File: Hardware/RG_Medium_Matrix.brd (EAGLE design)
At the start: 45.7 x 48.3 mm, 24 parts, among them IC1 74LS595D, IC2 74LS595D, U2 AVR_SPI_PRG_6PTH, U3 16MHz

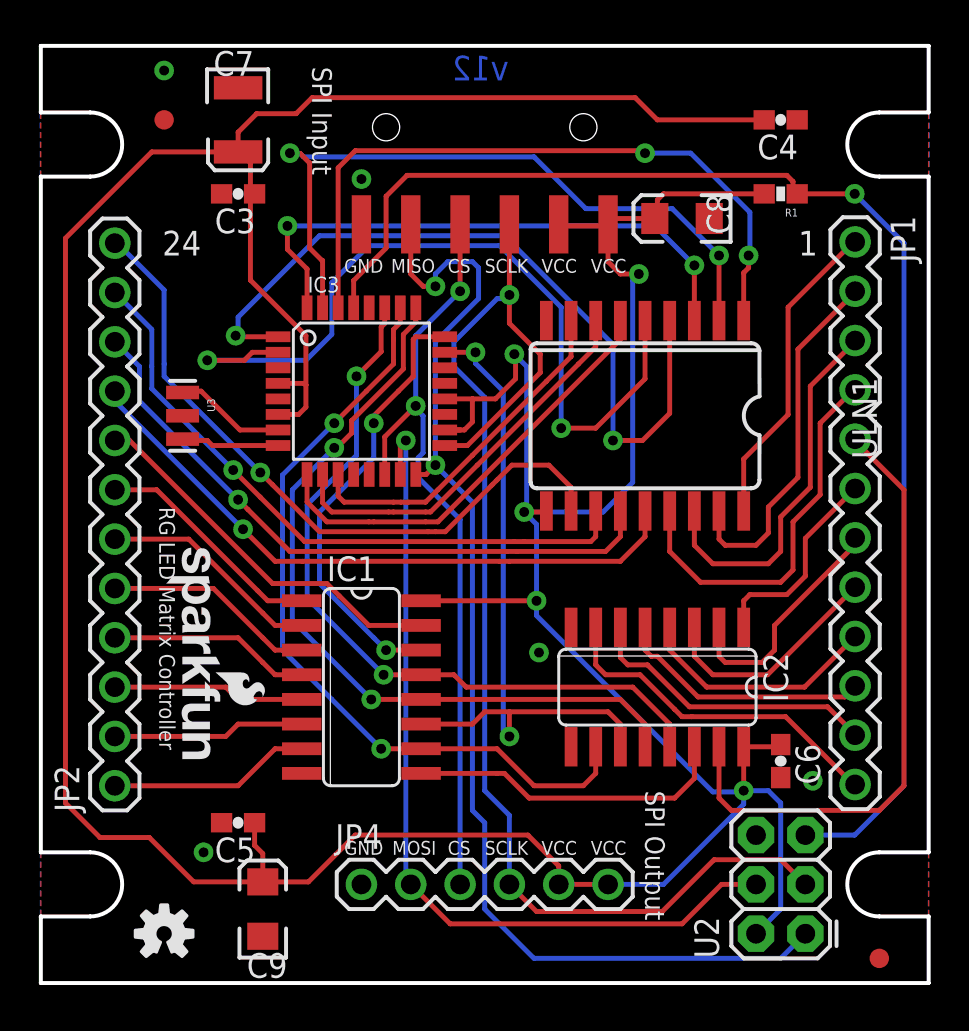
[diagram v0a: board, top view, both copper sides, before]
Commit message: Updating to locking footprints for SPI connectors
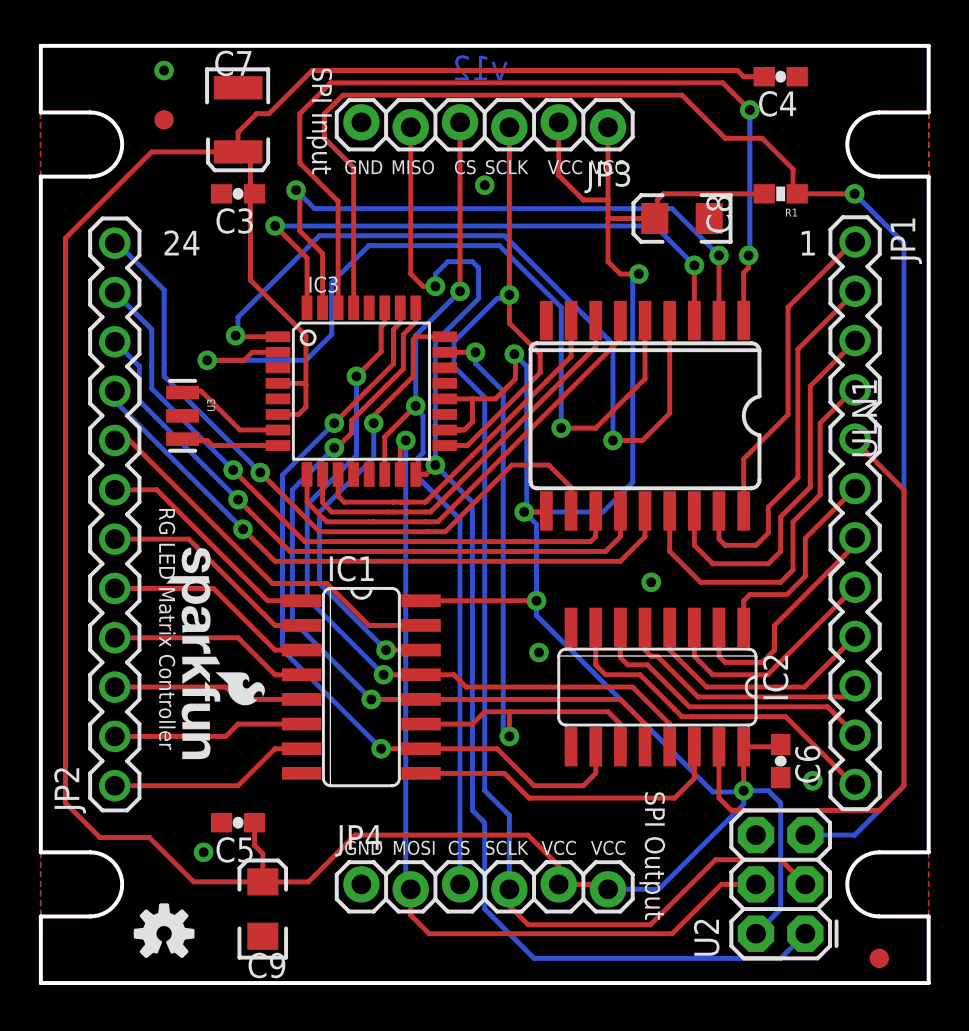
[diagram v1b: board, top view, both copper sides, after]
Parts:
- JP3: device SparkFun:1X06-SMD -> SparkFun-Connectors:1X06_LOCK
- JP4: device SparkFun:1X06 -> SparkFun-Connectors:1X06_LOCK
- moved JP3 6.35 mm to (29.2, 44.1)
- moved C4 2.22 mm to (38.1, 46.7)
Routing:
- net ROW1: track 35.8 -> 46.2 mm
- net RST: track 69.6 -> 79.2 mm
- net VCC: track 223.8 -> 232.6 mm
- net SCK: track 65.2 -> 71.4 mm
- net CS: track 40.3 -> 45.5 mm
- net MISO: track 61.6 -> 66.6 mm
- net ROW2: track 36.6 -> 33.2 mm
- net MOSI: track 44.5 -> 45.8 mm
- net ROW3: track 29.3 -> 30.2 mm
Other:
- board text added: "Ryan Owens"
- board text added: "Toni Klopfenstein"

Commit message: Switching to locking fp for 12 pin headers
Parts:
- JP1, JP2: value M12PTH -> M12LOCK; device SparkFun:1X12 -> SparkFun-Connectors:1X12_LOCK
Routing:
- net ROW_1: track 16.4 -> 17.1 mm

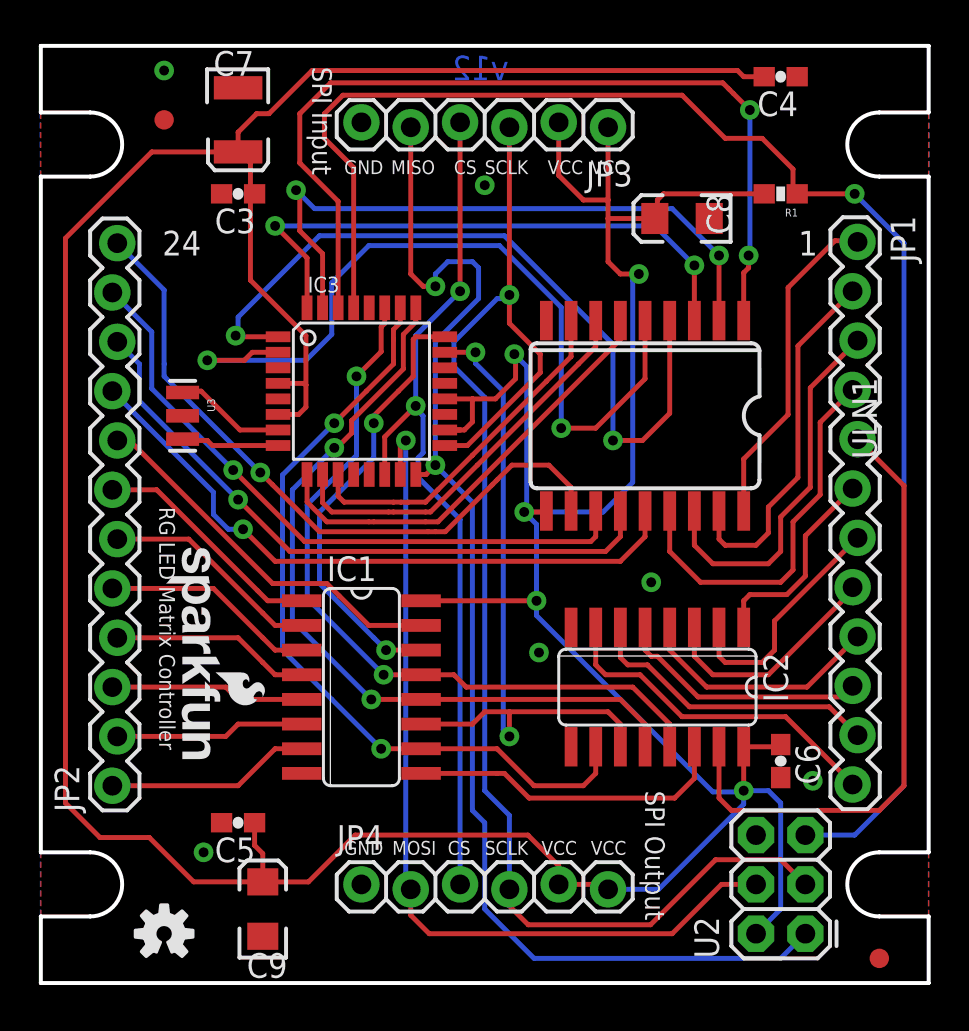
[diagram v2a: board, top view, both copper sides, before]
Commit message: Moving female header in to reduce gap between screens
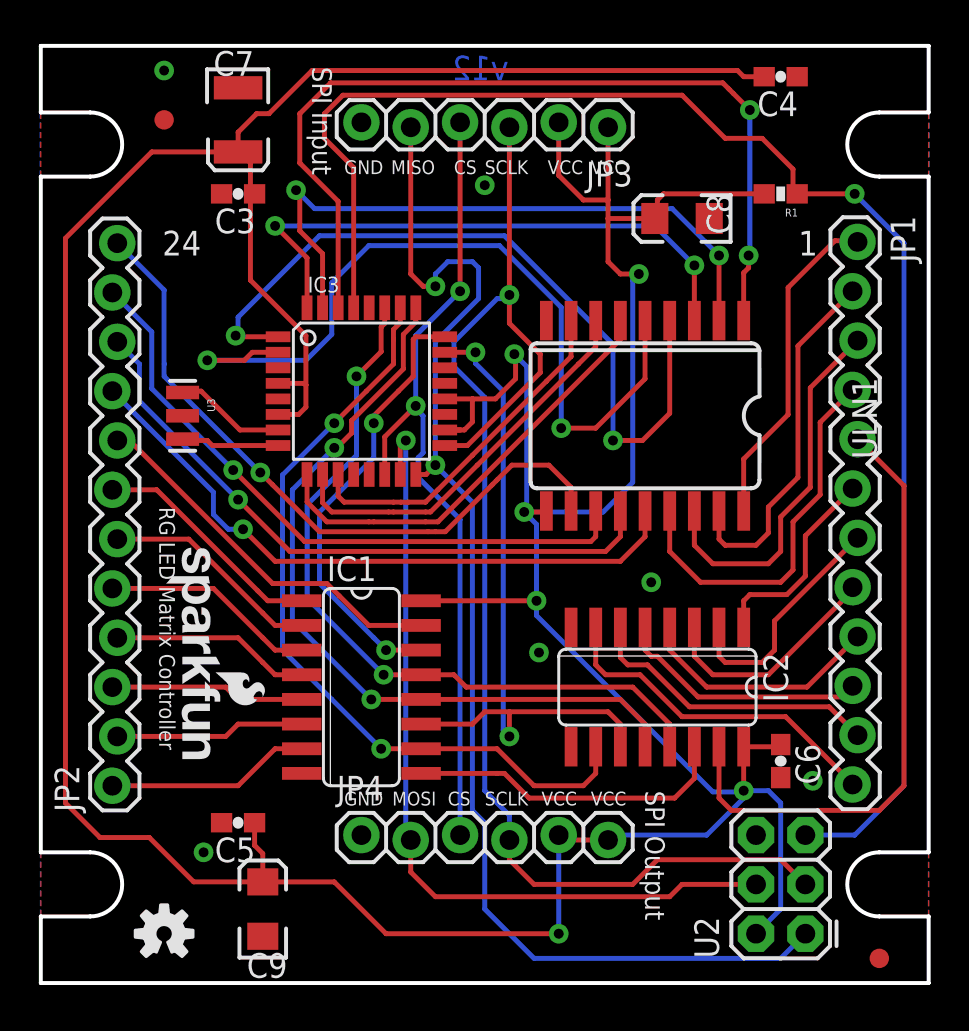
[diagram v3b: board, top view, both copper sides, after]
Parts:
- moved JP4 2.54 mm to (16.5, 7.62)
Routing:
- net SCK: track 71.4 -> 68.3 mm
- net MOSI: track 45.8 -> 42.9 mm
- net CS: track 45.5 -> 43.0 mm
- net VCC: track 232.6 -> 235.0 mm, vias 5 -> 6
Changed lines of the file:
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@@
 <text x="2.54" y="17.78" size="0.8128" layer="27" rot="R90">12-pin Female Header</text>
 <text x="45.72" y="31.75" size="0.8128" layer="27" rot="SR270">12-pin Female Header</text>
-<text x="15.621" y="6.604" size="0.7112" layer="21" font="vector" ratio="15">GND</text>
-<text x="18.0975" y="6.604" size="0.7112" layer="21" font="vector" ratio="15">MOSI</text>
-<text x="20.955" y="6.604" size="0.7112" layer="21" font="vector" ratio="15">CS</text>
-<text x="22.86" y="6.604" size="0.7112" layer="21" font="vector" ratio="15">SCLK</text>
-<text x="25.781" y="6.604" size="0.7112" layer="21" font="vector" ratio="15">VCC</text>
-<text x="28.321" y="6.604" size="0.7112" layer="21" font="vector" ratio="15">VCC</text>
+<text x="15.621" y="9.144" size="0.7112" layer="21" font="vector" ratio="15">GND</text>
+<text x="18.0975" y="9.144" size="0.7112" layer="21" font="vector" ratio="15">MOSI</text>
+<text x="20.955" y="9.144" size="0.7112" layer="21" font="vector" ratio="15">CS</text>
+<text x="22.86" y="9.144" size="0.7112" layer="21" font="vector" ratio="15">SCLK</text>
+<text x="25.781" y="9.144" size="0.7112" layer="21" font="vector" ratio="15">VCC</text>
+<text x="28.321" y="9.144" size="0.7112" layer="21" font="vector" ratio="15">VCC</text>
 <text x="15.621" y="41.656" size="0.7112" layer="21" font="vector" ratio="15">GND</text>
 <text x="18.034" y="41.656" size="0.7112" layer="21" font="vector" ratio="15">MISO</text>
@@
 </element>
 <element name="JP3" library="SparkFun-Connectors" package="1X06_LOCK" value="" x="29.21" y="44.069" rot="R180"/>
-<element name="JP4" library="SparkFun-Connectors" package="1X06_LOCK" value="" x="16.51" y="5.08"/>
+<element name="JP4" library="SparkFun-Connectors" package="1X06_LOCK" value="" x="16.51" y="7.62"/>
 <element name="U3" library="SparkFun" package="RESONATOR-SMD" value="16MHz" x="7.3025" y="29.21" rot="R270"/>
 <element name="LOGO1" library="SparkFun-Aesthetics" package="OSHW-LOGO-S" value="OSHW-LOGOS" x="6.35" y="2.54"/>
@@
 <wire x1="12.2174" y1="29.28" x2="13.278" y2="29.28" width="0.254" layer="1"/>
 <wire x1="20.8026" y1="28.48" x2="21.622" y2="28.48" width="0.254" layer="1"/>
-<wire x1="11.433" y1="5.207" x2="13.7795" y2="5.207" width="0.254" layer="1"/>
+<wire x1="11.433" y1="5.207" x2="15.113" y2="5.207" width="0.254" layer="1"/>
 <wire x1="11.01" y1="8.255" x2="11.01" y2="7.0875" width="0.254" layer="1"/>
 <wire x1="11.01" y1="7.0875" x2="11.43" y2="6.6675" width="0.254" layer="1"/>
@@
 <wire x1="34.6075" y1="9.8425" x2="36.1315" y2="9.8425" width="0.254" layer="16"/>
 <wire x1="36.1315" y1="9.8425" x2="36.195" y2="9.906" width="0.254" layer="16"/>
-<wire x1="36.195" y1="9.779" x2="36.195" y2="9.2075" width="0.254" layer="16"/>
-<wire x1="36.195" y1="9.2075" x2="31.8135" y2="4.826" width="0.254" layer="16"/>
 <wire x1="36.1315" y1="9.8425" x2="36.195" y2="9.779" width="0.254" layer="16"/>
-<wire x1="13.7795" y1="5.207" x2="16.1925" y2="7.62" width="0.254" layer="1"/>
-<wire x1="16.1925" y1="7.62" x2="25.0825" y2="7.62" width="0.254" layer="1"/>
-<wire x1="25.0825" y1="7.62" x2="26.67" y2="6.0325" width="0.254" layer="1"/>
-<wire x1="26.67" y1="6.0325" x2="26.67" y2="5.08" width="0.254" layer="1"/>
 <wire x1="28.956" y1="24.257" x2="30.48" y2="25.781" width="0.254" layer="16"/>
 <wire x1="13.6525" y1="33.3375" x2="13.6525" y2="30.7975" width="0.254" layer="1"/>
@@
 <wire x1="35.8775" y1="46.99" x2="36.195" y2="46.6725" width="0.254" layer="1"/>
 <wire x1="36.195" y1="46.6725" x2="37.25" y2="46.6725" width="0.254" layer="1"/>
-<wire x1="26.67" y1="5.08" x2="28.956" y2="5.08" width="0.254" layer="1"/>
-<wire x1="28.956" y1="5.08" x2="29.21" y2="4.826" width="0.254" layer="1"/>
-<wire x1="29.21" y1="4.826" x2="31.8135" y2="4.826" width="0.254" layer="16"/>
 <wire x1="26.67" y1="44.323" x2="26.67" y2="41.5925" width="0.254" layer="1"/>
 <wire x1="26.67" y1="41.5925" x2="27.94" y2="40.3225" width="0.254" layer="1"/>
 <wire x1="27.94" y1="40.3225" x2="29.21" y2="40.3225" width="0.254" layer="1"/>
+<wire x1="29.21" y1="7.366" x2="26.924" y2="7.366" width="0.254" layer="1"/>
+<wire x1="26.924" y1="7.366" x2="26.67" y2="7.62" width="0.254" layer="1"/>
+<wire x1="36.195" y1="9.779" x2="36.195" y2="9.525" width="0.254" layer="16"/>
+<wire x1="15.113" y1="5.207" x2="17.78" y2="2.54" width="0.254" layer="1"/>
+<wire x1="17.78" y1="2.54" x2="26.67" y2="2.54" width="0.254" layer="1"/>
+<via x="26.67" y="2.54" extent="1-16" drill="0.508"/>
+<wire x1="26.67" y1="2.54" x2="26.67" y2="7.62" width="0.254" layer="16"/>
+<wire x1="36.195" y1="9.525" x2="34.29" y2="7.62" width="0.254" layer="16"/>
+<wire x1="34.29" y1="7.62" x2="29.464" y2="7.62" width="0.254" layer="16"/>
+<wire x1="29.464" y1="7.62" x2="29.21" y2="7.366" width="0.254" layer="16"/>
 </signal>
 <signal name="RST">
@@
 <wire x1="18.796" y1="27.94" x2="18.51" y2="27.654" width="0.254" layer="1"/>
 <wire x1="18.669" y1="27.813" x2="18.796" y2="27.94" width="0.254" layer="16"/>
-<wire x1="35.052" y1="5.08" x2="36.83" y2="5.08" width="0.254" layer="1"/>
-<wire x1="32.512" y1="2.54" x2="35.052" y2="5.08" width="0.254" layer="1"/>
+<wire x1="33.02" y1="5.08" x2="36.83" y2="5.08" width="0.254" layer="1"/>
 <via x="18.796" y="27.94" extent="1-16" drill="0.508"/>
-<wire x1="18.796" y1="27.94" x2="18.796" y2="5.334" width="0.254" layer="16"/>
-<wire x1="19.05" y1="3.4925" x2="19.05" y2="4.826" width="0.254" layer="1"/>
-<wire x1="19.05" y1="4.826" x2="19.05" y2="5.08" width="0.254" layer="16"/>
-<wire x1="19.05" y1="5.08" x2="18.796" y2="5.334" width="0.254" layer="16"/>
-<wire x1="19.05" y1="3.4925" x2="20.0025" y2="2.54" width="0.254" layer="1"/>
-<wire x1="20.0025" y1="2.54" x2="32.512" y2="2.54" width="0.254" layer="1"/>
+<wire x1="18.796" y1="27.94" x2="18.796" y2="7.62" width="0.254" layer="16"/>
+<wire x1="18.796" y1="7.62" x2="19.05" y2="7.366" width="0.254" layer="16"/>
+<wire x1="33.02" y1="5.08" x2="32.385" y2="4.445" width="0.254" layer="1"/>
+<wire x1="32.385" y1="4.445" x2="20.32" y2="4.445" width="0.254" layer="1"/>
+<wire x1="20.32" y1="4.445" x2="19.05" y2="5.715" width="0.254" layer="1"/>
+<wire x1="19.05" y1="5.715" x2="19.05" y2="7.366" width="0.254" layer="1"/>
 </signal>
 <signal name="SCK">
@@
 <wire x1="24.13" y1="8.636" x2="22.86" y2="9.906" width="0.254" layer="16"/>
 <wire x1="22.86" y1="9.906" x2="22.86" y2="30.1625" width="0.254" layer="16"/>
-<wire x1="24.13" y1="4.826" x2="24.13" y2="8.636" width="0.254" layer="16"/>
+<wire x1="24.13" y1="7.366" x2="24.13" y2="8.636" width="0.254" layer="16"/>
 <wire x1="38.1" y1="6.35" x2="39.37" y2="5.08" width="0.254" layer="1"/>
 <via x="24.13" y="35.433" extent="1-16" drill="0.508"/>
@@
 <wire x1="23.495" y1="35.2425" x2="23.9395" y2="35.2425" width="0.254" layer="16"/>
 <wire x1="23.9395" y1="35.2425" x2="24.13" y2="35.433" width="0.254" layer="16"/>
-<wire x1="38.1" y1="6.35" x2="34.75" y2="6.35" width="0.254" layer="1"/>
-<wire x1="34.75" y1="6.35" x2="31.4" y2="3" width="0.254" layer="1"/>
-<wire x1="31.4" y1="3" x2="25.1" y2="3" width="0.254" layer="1"/>
-<wire x1="25.1" y1="3" x2="24.1" y2="4" width="0.254" layer="1"/>
-<wire x1="24.1" y1="4" x2="24.1" y2="4.796" width="0.254" layer="1"/>
-<wire x1="24.1" y1="4.796" x2="24.13" y2="4.826" width="0.254" layer="1"/>
+<wire x1="38.1" y1="6.35" x2="31.75" y2="6.35" width="0.254" layer="1"/>
+<wire x1="31.75" y1="6.35" x2="30.48" y2="5.08" width="0.254" layer="1"/>
+<wire x1="30.48" y1="5.08" x2="25.4" y2="5.08" width="0.254" layer="1"/>
+<wire x1="25.4" y1="5.08" x2="24.13" y2="6.35" width="0.254" layer="1"/>
+<wire x1="24.13" y1="6.35" x2="24.13" y2="7.366" width="0.254" layer="1"/>
 </signal>
 <signal name="MISO">
@@
 <wire x1="19.685" y1="29.21" x2="19.304" y2="29.591" width="0.254" layer="16"/>
 <wire x1="19.304" y1="29.591" x2="19.304" y2="29.718" width="0.254" layer="16"/>
-<wire x1="21.59" y1="5.08" x2="21.59" y2="23.876" width="0.254" layer="16"/>
+<wire x1="21.59" y1="7.62" x2="21.59" y2="23.876" width="0.254" layer="16"/>
 <via x="21.59" y="35.6235" extent="1-16" drill="0.508"/>
 <via x="19.304" y="29.718" extent="1-16" drill="0.508"/>
